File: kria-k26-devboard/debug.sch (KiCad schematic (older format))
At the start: 68 parts, among them J8 USB4105-GF-A, J9 0878311420, Q10 DTC014TEBTL, Q17 DTC014TEBTL, Q9 DTC014TEBTL, U28 WE-TVS-82400152, U29 MIC5211-3.3YM6-TR, U30 FT4232HPQ, U31 93LC56CT-IMC, U32 74AVC4T245RSVRG4, U33 74AVC4T245RSVRG4, U34 SN74AVC2T245RSWR, U35 SN74AVC2T245RSWR, U36 NC7WZ07P6X, U54 TPD4E05U06QDQARQ1, Y5 ABM8G-12.000MHZ-18-D2Y-T

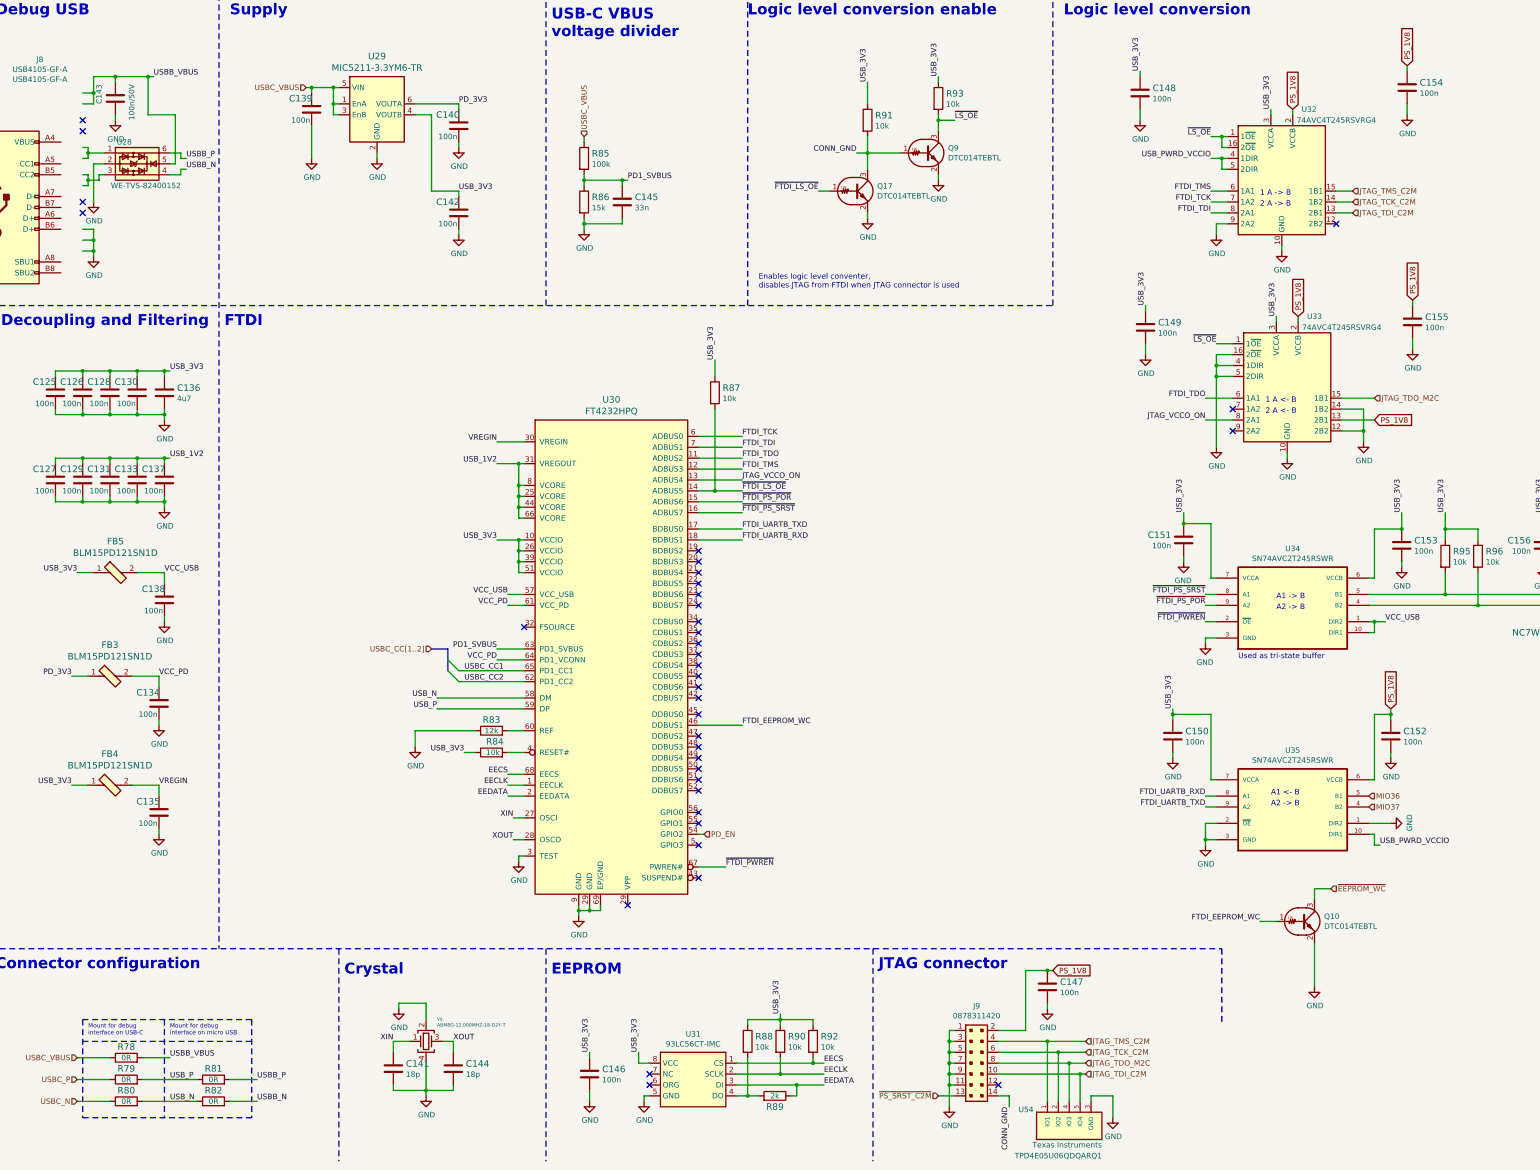
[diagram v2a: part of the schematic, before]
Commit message: Fixed possible FTDI-USB backfeeding issue, finished PS and FTDI power planes creation, finished routing of FTDI/Debug part
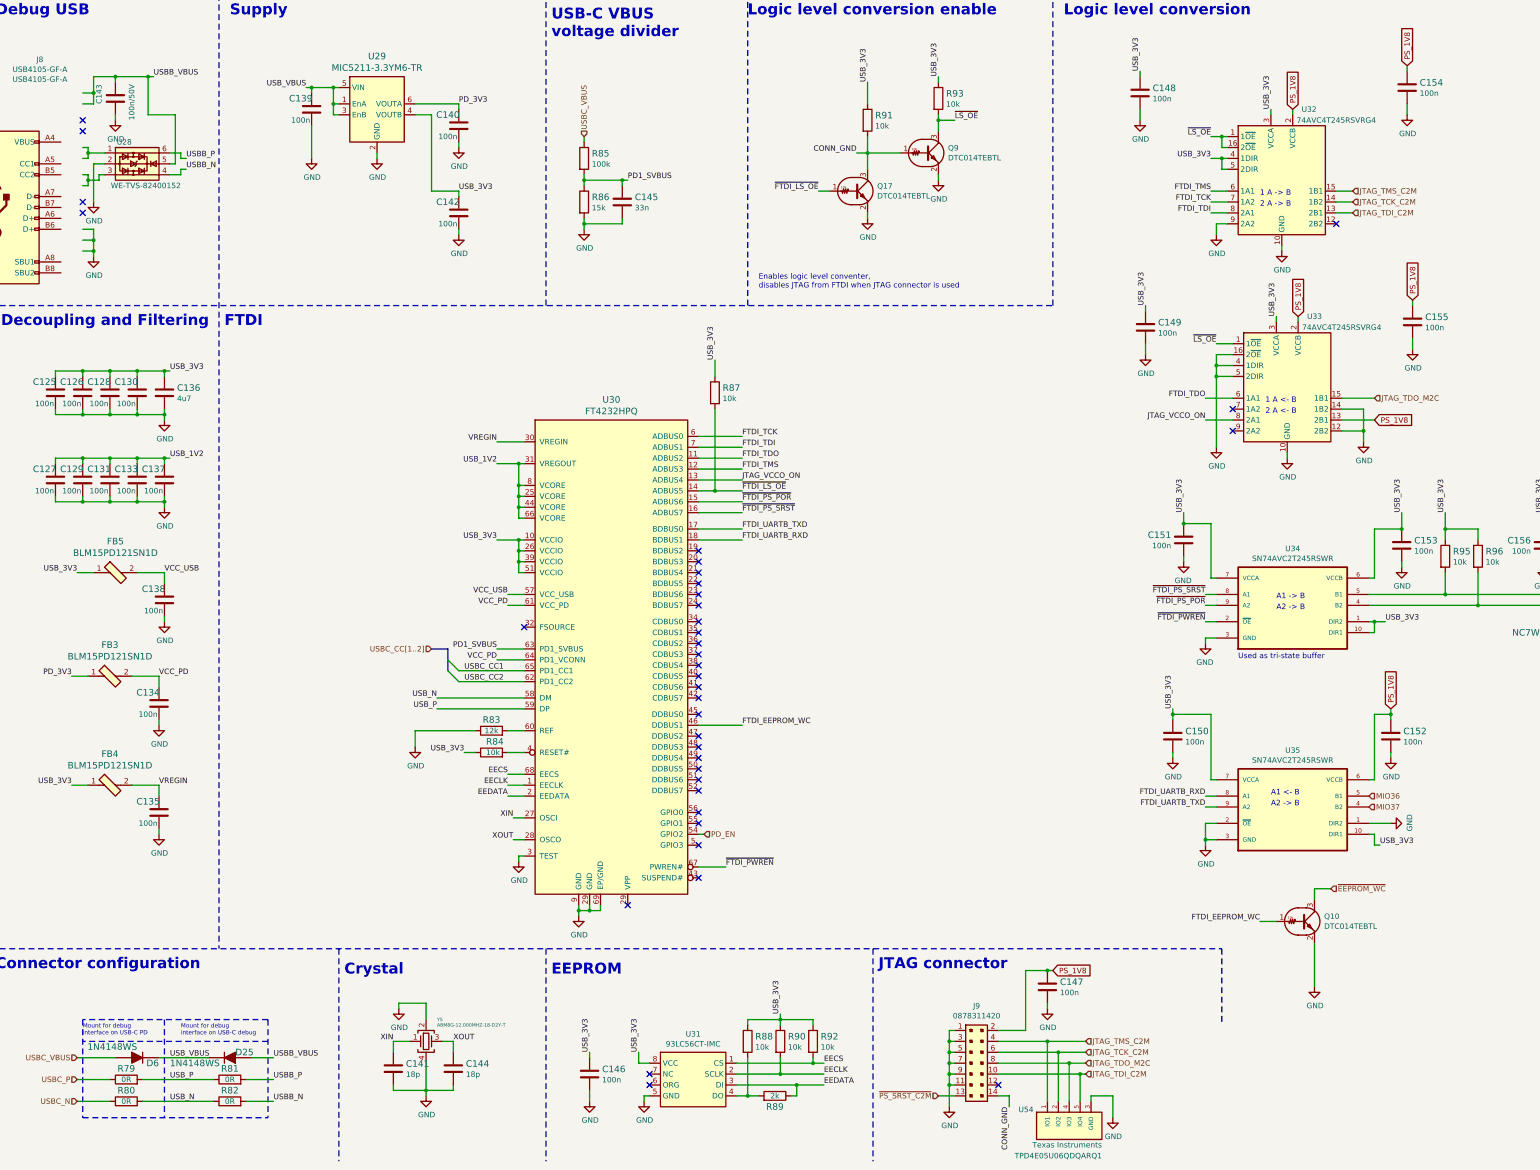
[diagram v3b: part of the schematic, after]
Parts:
- removed R78: R_0R_0402, antmicro-footprints:0402-res, symbol antmicroResistors0402:R_0R_0402
- added D25, D6: 1N4148WS, antmicro-footprints:SOD-323F, symbol antmicroDiodesRectifiersSingle:1N4148WS
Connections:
- net USB_PWRD_VCCIO is gone; now on net USB_3V3: U32.4 (1DIR), U32.5 (2DIR), U35.10 (DIR1)
- net USBB_VBUS: now also D25.A
- net USBC_VBUS: now also D6.A; no longer C139.2, U29.1 (EnA), U29.3 (EnB), U29.5 (VIN)
- net USB_3V3: now also U34.1 (DIR2), U34.10 (DIR1)
- net VCC_USB: no longer U34.1 (DIR2), U34.10 (DIR1)
- new net USB_VBUS: C139.2, D25.K, D6.K, U29.1 (EnA), U29.3 (EnB), U29.5 (VIN)
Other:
- note added: "Mount for debug \ninterface on USB-C PD"
- note added: "Mount for debug \ninterface on USB-C debug"
- note removed: "Mount for debug \ninterface on USB-C"
- note removed: "Mount for debug \ninterface on micro USB"
- moved on the sheet: R81, R82
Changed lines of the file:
@@
 Wire Wire Line
 	11750 3800 11900 3800
-Text Label 11700 2000 2    50   ~ 0
-USB_PWRD_VCCIO
 Wire Wire Line
 	11700 2000 11800 2000
@@
 Text Label 11650 7850 2    50   ~ 0
 FTDI_UARTB_RXD
-Text Label 13250 8300 0    50   ~ 0
-USB_PWRD_VCCIO
 $Comp
 L power:GND #PWR0335
@@
 Wire Wire Line
 	3450 2000 3450 1700
-Text HLabel 3400 1350 0    50   Input ~ 0
-USBC_VBUS
 Wire Wire Line
 	3400 1350 3450 1350
@@
 Wire Wire Line
 	4400 1500 4800 1500
-Text HLabel 5950 1800 1    50   Input ~ 0
-USBC_VBUS
 $Comp
 L antmicroResistors0402:R_0R_0402 R82
 U 1 1 65D83F07
-P 2550 10650
-F 0 "R82" H 2550 10750 60  0000 C CNN
-F 1 "R_0R_0402" H 2550 10500 60  0001 C CNN
-F 2 "antmicro-footprints:0402-res" H 2750 10850 60  0001 L CNN
-F 3 "" H 2550 10650 50  0001 C CNN
-F 4 "PANASONIC" H 2750 11050 60  0001 L CNN "Manufacturer"
-F 5 "ERJ2GE0R00X" H 2750 10950 60  0001 L CNN "MPN"
-F 6 "0R" H 2550 10650 50  0000 C CNN "Val"
-	1    2550 10650
+P 2700 10650
+F 0 "R82" H 2700 10750 60  0000 C CNN
+F 1 "R_0R_0402" H 2700 10500 60  0001 C CNN
+F 2 "antmicro-footprints:0402-res" H 2900 10850 60  0001 L CNN
+F 3 "" H 2700 10650 50  0001 C CNN
+F 4 "PANASONIC" H 2900 11050 60  0001 L CNN "Manufacturer"
+F 5 "ERJ2GE0R00X" H 2900 10950 60  0001 L CNN "MPN"
+F 6 "0R" H 2700 10650 50  0000 C CNN "Val"
+	1    2700 10650
 	1    0    0    -1
 $EndComp
@@
 USBC_P
 Wire Wire Line
-	2950 10450 2700 10450
+	3100 10450 2850 10450
 Wire Wire Line
 	1600 10450 1300 10450
@@
 Text Label 4600 6950 2    50   ~ 0
 USB_N
-Text Label 2950 10450 0    50   ~ 0
+Text Label 3100 10450 0    50   ~ 0
 USBB_P
 Text Label 5150 6600 2    50   ~ 0
@@
 Wire Wire Line
 	7000 8200 7050 8200
-$Comp
-L antmicroResistors0402:R_0R_0402 R78
-U 1 1 6615CA96
-P 1750 10250
-F 0 "R78" H 1750 10350 60  0000 C CNN
-F 1 "R_0R_0402" H 1750 10100 60  0001 C CNN
-F 2 "antmicro-footprints:0402-res" H 1950 10450 60  0001 L CNN
-F 3 "" H 1750 10250 50  0001 C CNN
-F 4 "PANASONIC" H 1950 10650 60  0001 L CNN "Manufacturer"
-F 5 "ERJ2GE0R00X" H 1950 10550 60  0001 L CNN "MPN"
-F 6 "0R" H 1750 10250 50  0000 C CNN "Val"
-	1    1750 10250
-	1    0    0    -1
-$EndComp
 Text Label 2150 10250 0    50   ~ 0
-USBB_VBUS
+USB_VBUS
 Text HLabel 1300 10250 0    50   Input ~ 0
 USBC_VBUS
 Text HLabel 7050 8200 2    50   Input ~ 0
 PD_EN
-Text Label 2950 10650 0    50   ~ 0
+Text Label 3100 10650 0    50   ~ 0
 USBB_N
 Text Label 2150 10650 0    50   ~ 0
@@
 	1600 10650 1300 10650
 Wire Wire Line
-	2950 10650 2700 10650
+	3100 10650 2850 10650
 Text HLabel 1300 10650 0    50   Input ~ 0
 USBC_N
@@
 L antmicroResistors0402:R_0R_0402 R81
 U 1 1 65DA9332
-P 2550 10450
-F 0 "R81" H 2550 10550 60  0000 C CNN
-F 1 "R_0R_0402" H 2550 10300 60  0001 C CNN
-F 2 "antmicro-footprints:0402-res" H 2750 10650 60  0001 L CNN
-F 3 "" H 2550 10450 50  0001 C CNN
-F 4 "PANASONIC" H 2750 10850 60  0001 L CNN "Manufacturer"
-F 5 "ERJ2GE0R00X" H 2750 10750 60  0001 L CNN "MPN"
-F 6 "0R" H 2550 10450 50  0000 C CNN "Val"
-	1    2550 10450
-	1    0    0    -1
-$EndComp
-Wire Wire Line
-	1900 10450 2400 10450
-Wire Wire Line
-	1900 10650 2400 10650
-Wire Wire Line
-	1900 10250 2150 10250
+P 2700 10450
+F 0 "R81" H 2700 10550 60  0000 C CNN
+F 1 "R_0R_0402" H 2700 10300 60  0001 C CNN
+F 2 "antmicro-footprints:0402-res" H 2900 10650 60  0001 L CNN
+F 3 "" H 2700 10450 50  0001 C CNN
+F 4 "PANASONIC" H 2900 10850 60  0001 L CNN "Manufacturer"
+F 5 "ERJ2GE0R00X" H 2900 10750 60  0001 L CNN "MPN"
+F 6 "0R" H 2700 10450 50  0000 C CNN "Val"
+	1    2700 10450
+	1    0    0    -1
+$EndComp
+Wire Wire Line
+	1900 10450 2550 10450
+Wire Wire Line
+	1900 10650 2550 10650
 Wire Notes Line
-	1350 10800 2900 10800
+	1350 10800 3050 10800
 Wire Notes Line
-	2900 9900 1350 9900
+	3050 9900 1350 9900
 Wire Notes Line
-	2900 10100 1350 10100
+	3050 10100 1350 10100
 Wire Notes Line
 	1350 9900 1350 10800
@@
 	2100 9900 2100 10800
 Wire Notes Line
-	2900 9900 2900 10800
-Text Notes 1400 10050 0    39   ~ 0
-Mount for debug \ninterface on USB-C
-Text Notes 2150 10050 0    39   ~ 0
-Mount for debug \ninterface on micro USB
+	3050 9900 3050 10800
+Text Notes 1350 10050 0    39   ~ 0
+Mount for debug \ninterface on USB-C PD
+Text Notes 2250 10050 0    39   ~ 0
+Mount for debug \ninterface on USB-C debug
 Text Label 4850 7450 2    50   ~ 0
 USB_3V3
@@
 $EndComp
 Wire Wire Line
-	1300 10250 1600 10250
-Wire Wire Line
 	1350 2650 1450 2650
 Wire Wire Line
@@
 Wire Wire Line
 	13200 8300 13250 8300
+Text Label 3400 1350 2    50   ~ 0
+USB_VBUS
+Text Label 3100 10250 0    50   ~ 0
+USBB_VBUS
+Text HLabel 5950 1800 1    50   Input ~ 0
+USBC_VBUS
+Wire Wire Line
+	2900 10250 3100 10250
+$Comp
+L antmicroDiodesRectifiersSingle:1N4148WS D?
+U 1 1 63741A22
+P 1850 10250
+AR Path="/63C44BC2/629B9728/63741A22" Ref="D?"  Part="1"
+AR Path="/625B0244/63741A22" Ref="D6"  Part="1"
+F 0 "D6" H 2050 10200 60  0000 R CNN
+F 1 "1N4148WS" H 1850 10350 60  0000 R CNN
+F 2 "antmicro-footprints:SOD-323F" H 2050 10450 60  0001 L CNN
+F 3 "https://www.onsemi.com/pub/Collateral/1N914BWS-D.pdf" H 2050 10550 60  0001 L CNN
+F 4 "1N4148WS" H 2050 10750 60  0001 L CNN "MPN"
+F 5 "ON Semiconductor" H 2050 11350 60  0001 L CNN "Manufacturer"
+	1    1850 10250
+	1    0    0    -1
+$EndComp
+$Comp
+L antmicroDiodesRectifiersSingle:1N4148WS D?
+U 1 1 6376D6F3
+P 2700 10250
+AR Path="/63C44BC2/629B9728/6376D6F3" Ref="D?"  Part="1"
+AR Path="/625B0244/6376D6F3" Ref="D25"  Part="1"
+F 0 "D25" H 2650 10200 60  0000 R CNN
+F 1 "1N4148WS" H 3250 10300 60  0000 R CNN
+F 2 "antmicro-footprints:SOD-323F" H 2900 10450 60  0001 L CNN
+F 3 "https://www.onsemi.com/pub/Collateral/1N914BWS-D.pdf" H 2900 10550 60  0001 L CNN
+F 4 "1N4148WS" H 2900 10750 60  0001 L CNN "MPN"
+F 5 "ON Semiconductor" H 2900 11350 60  0001 L CNN "Manufacturer"
+	1    2700 10250
+	-1   0    0    1
+$EndComp
+Wire Wire Line
+	1300 10250 1650 10250
+Wire Wire Line
+	2050 10250 2500 10250
+Text Label 13250 8300 0    50   ~ 0
+USB_3V3
 Text Label 13300 6250 0    50   ~ 0
-VCC_USB
+USB_3V3
 Wire Bus Line
 	4700 6500 4700 6700
+Text Label 11700 2000 2    50   ~ 0
+USB_3V3
 $EndSCHEMATC

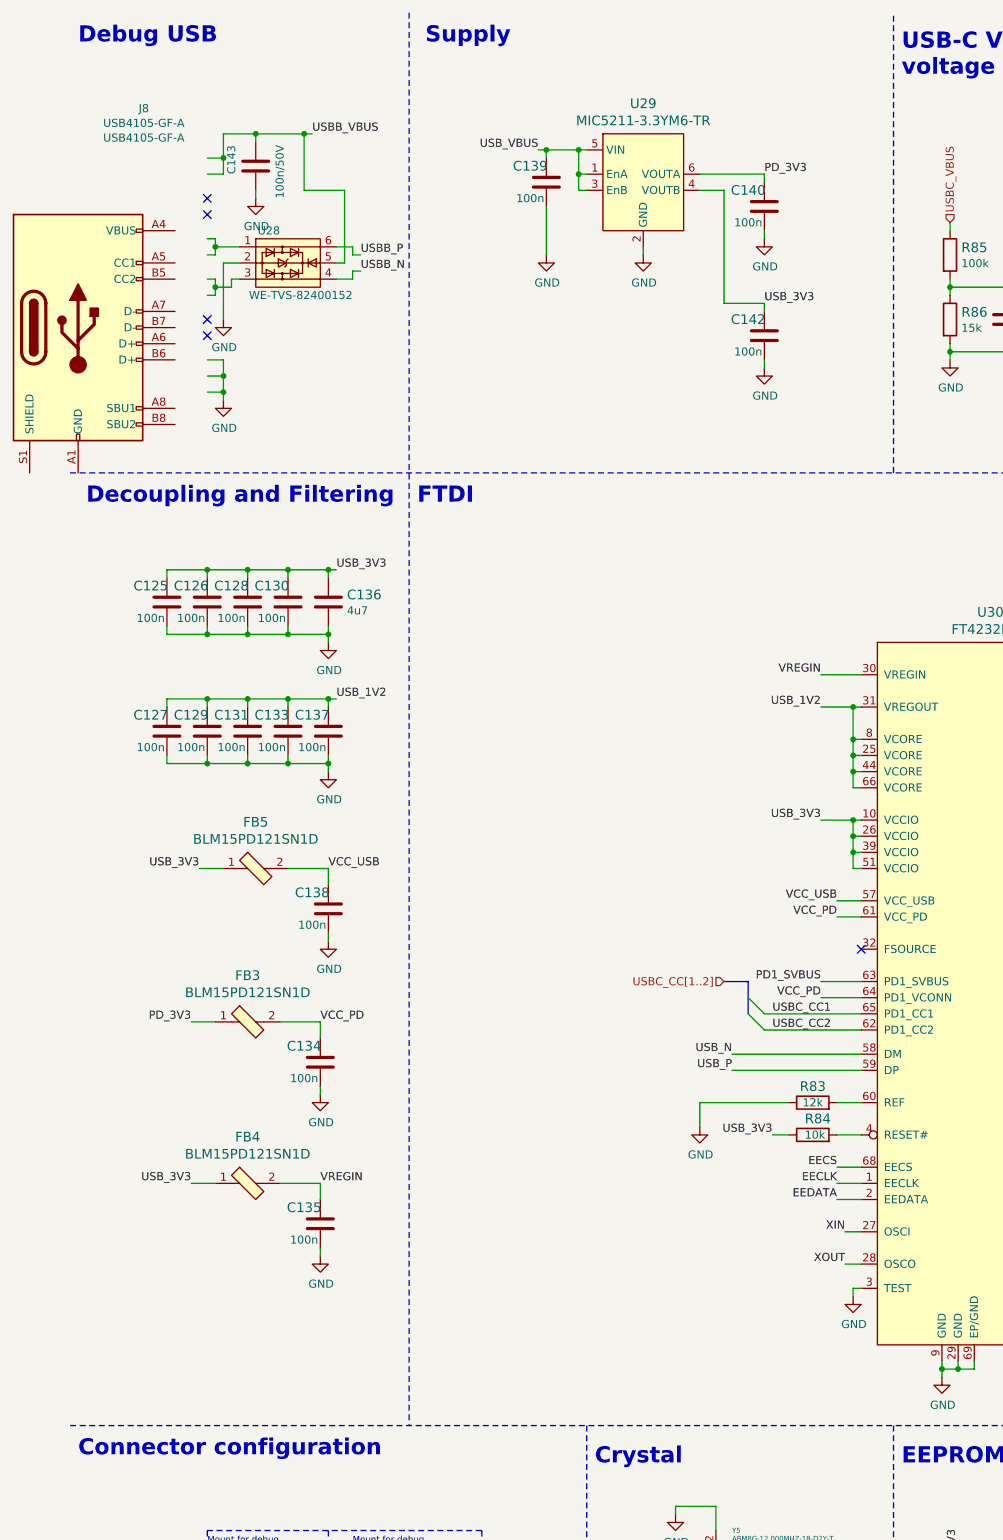
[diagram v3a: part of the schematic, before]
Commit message: Finished Power planes and overall connectivity
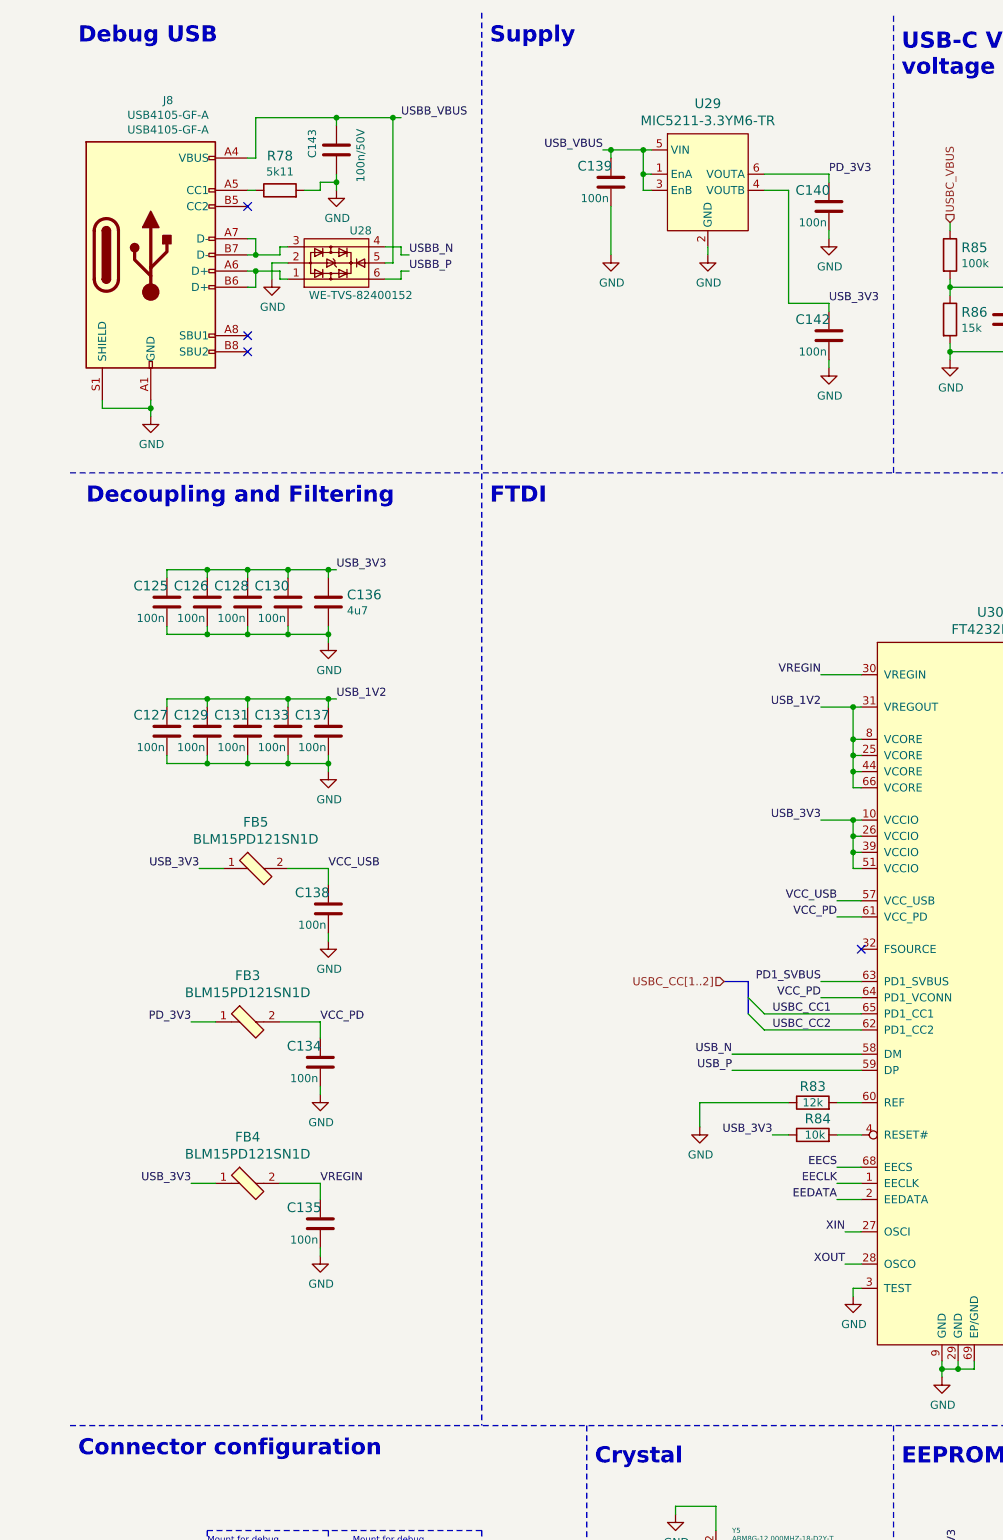
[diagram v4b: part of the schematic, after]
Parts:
- added R78: R_5k11_0402, antmicro-footprints:0402-res, symbol antmicroResistors0402:R_5k11_0402
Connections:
- net GND: now also J8.A1 (GND), J8.A12 (GND), J8.B1 (GND), J8.B12 (GND), J8.S1 (SHIELD), R78.2
- net USBB_VBUS: now also J8.A4 (VBUS), J8.A9 (VBUS), J8.B4 (VBUS), J8.B9 (VBUS)
- net at U28.1: now also J8.A6 (D+), J8.B6 (D+)
- net at U28.3: now also J8.A7 (D-), J8.B7 (D-)
- net at J8.A5 (CC1): now also R78.1
- no-connect marks 37 -> 36
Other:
- moved on the sheet: C139, C140, C142, C143, J8, U28, U29
